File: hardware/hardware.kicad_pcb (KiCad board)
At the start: 2 copper layers, 32 parts, among them J1 Conn_01x02, J3 USB_B_Micro, J4 Conn_01x02, J5 Conn_01x02, J6 Conn_01x02, J7 Conn_01x06, Q1 BSS138, Q2 BSS138, U1 CH340C, U2 ESP32-WROOM-32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

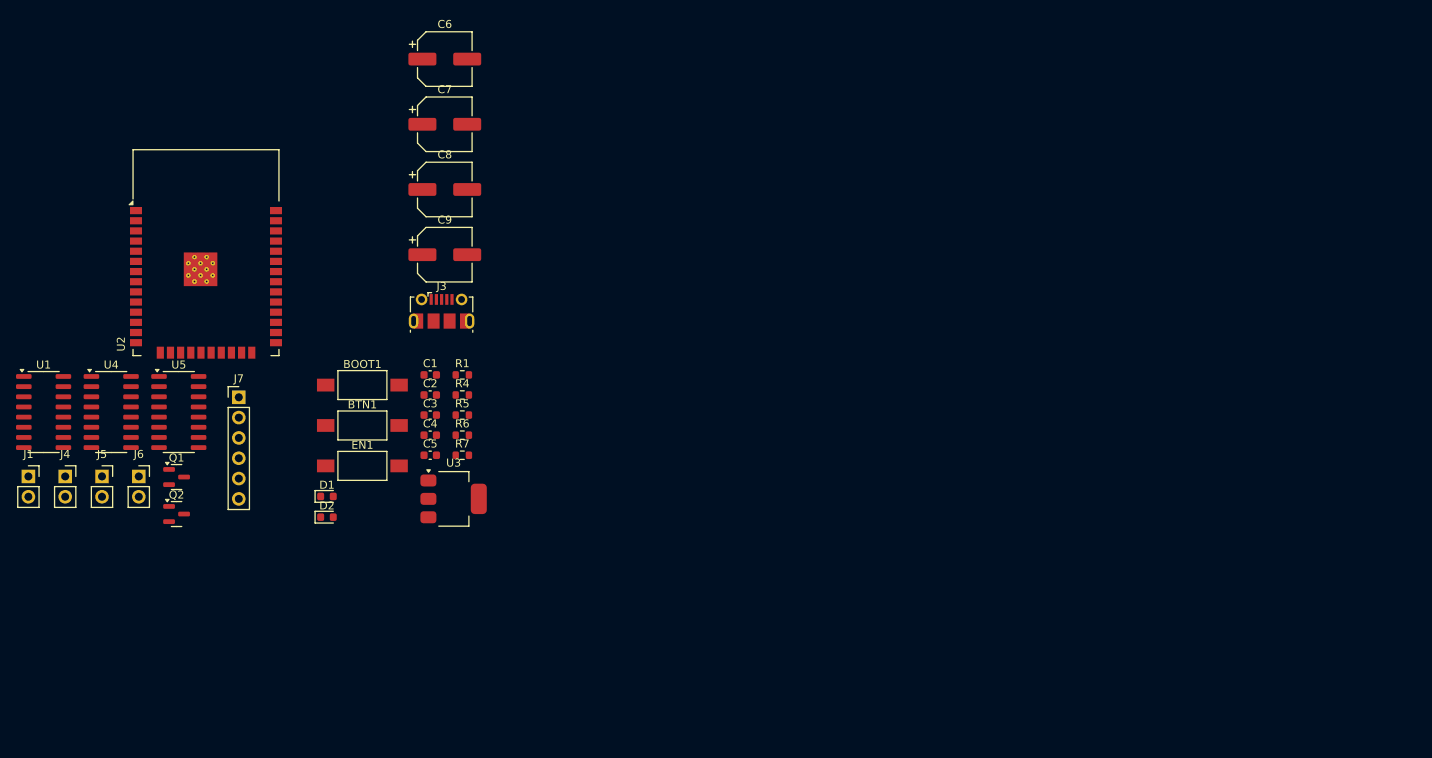
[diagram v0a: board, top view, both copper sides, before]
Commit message: place componants + mounting holes
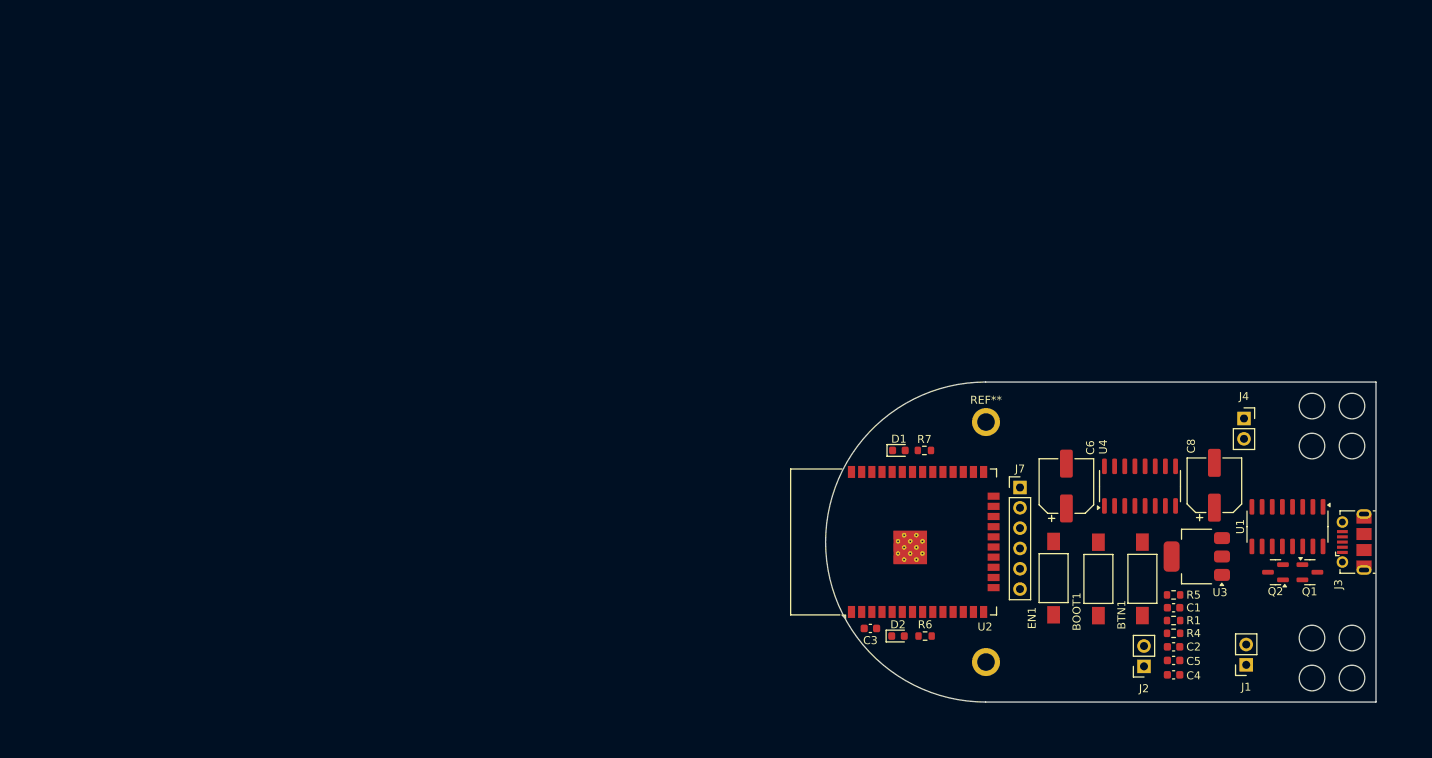
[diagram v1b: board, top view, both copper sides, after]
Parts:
- removed C7, C9: C_Polarized_Small, Capacitor_SMD:CP_Elec_6.3x4.9
- removed J5, J6: Conn_01x02, Connector_PinSocket_2.54mm:PinSocket_1x02_P2.54mm_Vertical
- removed U5: MX1508, Package_SO:SOIC-16_3.9x9.9mm_P1.27mm
- added ?: , , F.Cu at (156.2, 100.0)
- added J2: Conn_01x02, Connector_PinSocket_2.54mm:PinSocket_1x02_P2.54mm_Vertical, F.Cu at (176.0, 100.5)
- added REF**: MountingHole_2.2mm_M2_ISO7380_Pad, MountingHole:MountingHole_2.2mm_M2_ISO7380_Pad, F.Cu at (156.2, 70.0)
- moved U1 156.1 mm to (193.9, 83.1), turned to -90 degrees
- moved J1 154.0 mm to (188.8, 100.3), turned to 180 degrees
- moved J4 147.5 mm to (188.5, 69.6)
- moved Q1 142.2 mm to (196.7, 88.8)
- moved Q2 137.6 mm to (192.4, 88.8), turned to 180 degrees
- moved U4 128.9 mm to (175.5, 78.0), turned to 90 degrees
- moved J3 117.7 mm to (202.3, 85.0), turned to 90 degrees
- moved C8 103.1 mm to (184.8, 77.9), turned to 90 degrees
- moved BTN1 99.4 mm to (175.8, 89.6), turned to 90 degrees
- moved J7 98.3 mm to (160.5, 78.2)
- moved C2 98.1 mm to (179.7, 98.1)
- moved C4 97.6 mm to (179.7, 101.6), turned to 180 degrees
- moved C1 97.4 mm to (179.7, 93.2), turned to 180 degrees
- moved C5 96.4 mm to (179.7, 99.8), turned to 180 degrees
- moved BOOT1 95.1 mm to (170.3, 89.6), turned to 90 degrees
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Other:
- board outline added: 68.8 x 40 mm

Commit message: wiring pcb
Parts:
- moved C2 6.43 mm to (173.4, 99.4), turned to 90 degrees
- moved C4 2.03 mm to (179.7, 99.6), turned to 0 degrees
- moved C5 1.80 mm to (179.7, 98.0)
- moved D1 0.39 mm to (145.0, 73.4)
- moved R7 0.38 mm to (148.2, 73.4)
- turned R4 to 0 degrees
- turned R6 to 180 degrees
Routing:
- net +5V: track 0.00 -> 94.8 mm, vias 0 -> 5
- net +3V3: track 0.00 -> 86.8 mm
- net ESP32_EN: track 0.00 -> 75.7 mm, vias 0 -> 4
- net TX-PROG: track 0.00 -> 66.9 mm, vias 0 -> 2
- net RX-PROG: track 0.00 -> 65.4 mm, vias 0 -> 2
- net ESP32_IO0: track 0.00 -> 55.1 mm, vias 0 -> 2
- net Net-(J1-Pin_1): track 0.00 -> 39.4 mm, vias 0 -> 1
- net Net-(J1-Pin_2): track 0.00 -> 31.3 mm, vias 0 -> 1
- net BTN1: track 0.00 -> 28.4 mm
- net Net-(J4-Pin_1): track 0.00 -> 21.9 mm
- net Net-(U2-IO13): track 0.00 -> 20.3 mm, vias 0 -> 2
- net Net-(J4-Pin_2): track 0.00 -> 16.8 mm
- net GND: track 0.00 -> 12.6 mm, vias 0 -> 35
- net D-: track 0.00 -> 12.1 mm
- net D+: track 0.00 -> 10.6 mm
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- added copper zone on B.Cu, net GND
- added copper zone on F.Cu, net GND

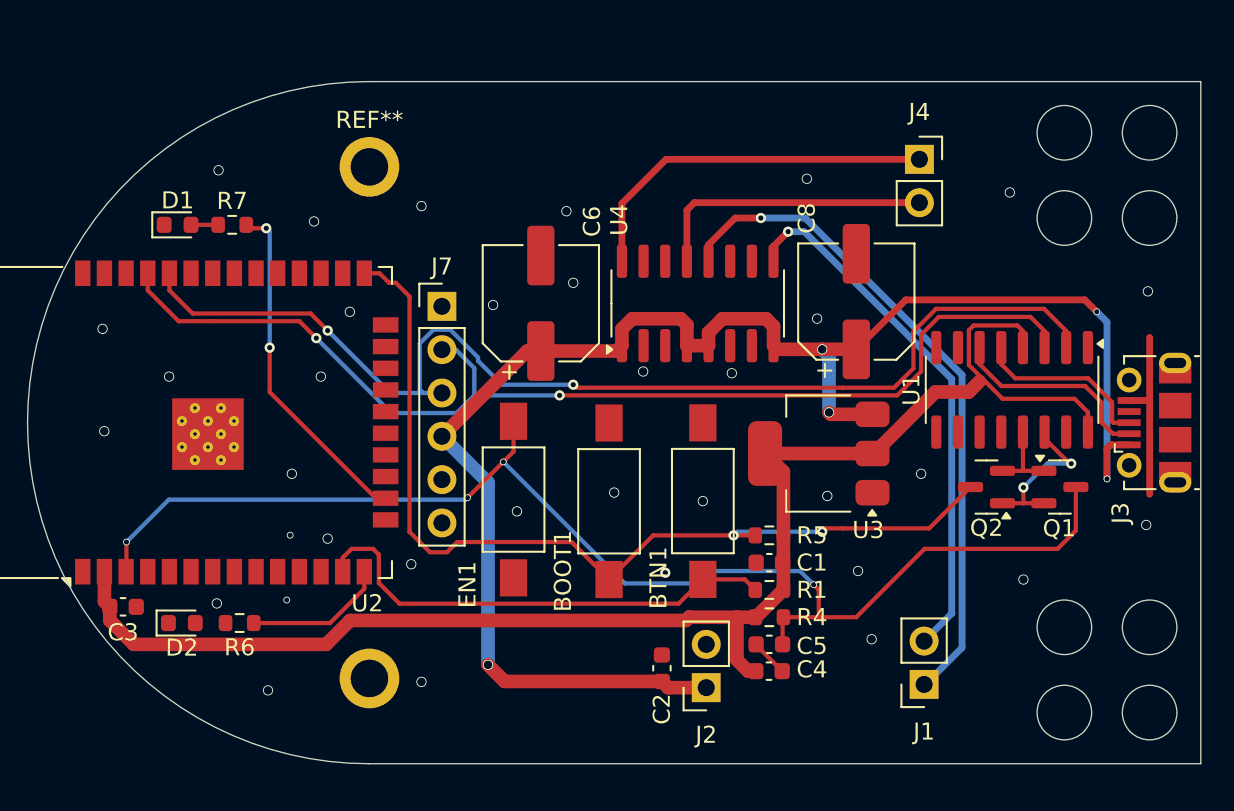
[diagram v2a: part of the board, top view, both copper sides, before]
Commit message: add wiring mx1508 + vcc headers connector
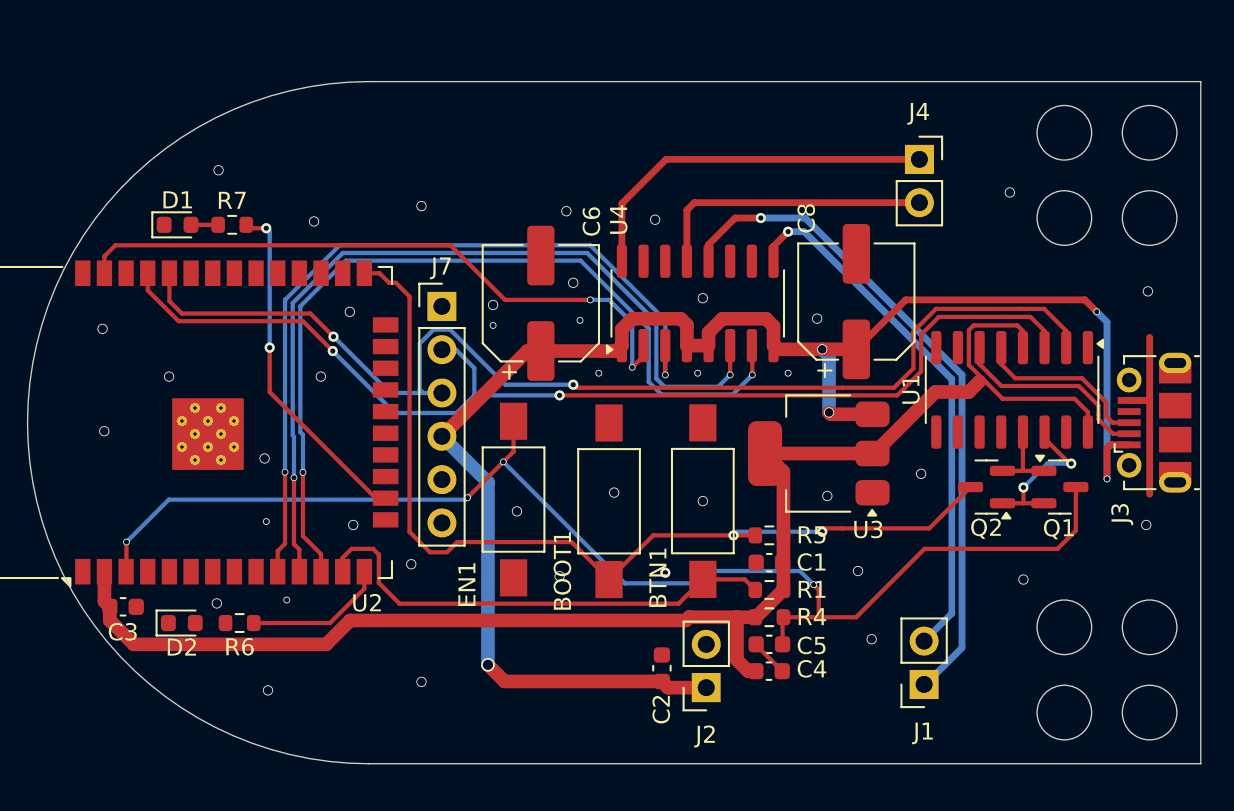
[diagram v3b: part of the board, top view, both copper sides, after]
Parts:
- removed ?: , 
- removed REF**: MountingHole_2.2mm_M2_ISO7380_Pad, MountingHole:MountingHole_2.2mm_M2_ISO7380_Pad
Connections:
- U2 pad 10: unconnected-(U2-IO25-Pad10) -> MTR_L_2
- U2 pad 11: unconnected-(U2-IO26-Pad11) -> MTR_R_1
- U2 pad 12: unconnected-(U2-IO27-Pad12) -> MTR_R_2
- U2 pad 37: unconnected-(U2-IO23-Pad37) -> MTR_L_1
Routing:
- net MTR_R_2: track 0.00 -> 50.3 mm, vias 0 -> 2
- net MTR_R_1: track 0.00 -> 50.0 mm, vias 0 -> 2
- net MTR_L_2: track 0.00 -> 46.5 mm, vias 0 -> 2
- net MTR_L_1: track 0.00 -> 38.3 mm, vias 0 -> 2
- net GND: vias 35 -> 40
